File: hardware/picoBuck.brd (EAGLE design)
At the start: 22.8 x 27.3 mm, 23 parts, among them U1 AL8805, U2 AL8805, U3 AL8805

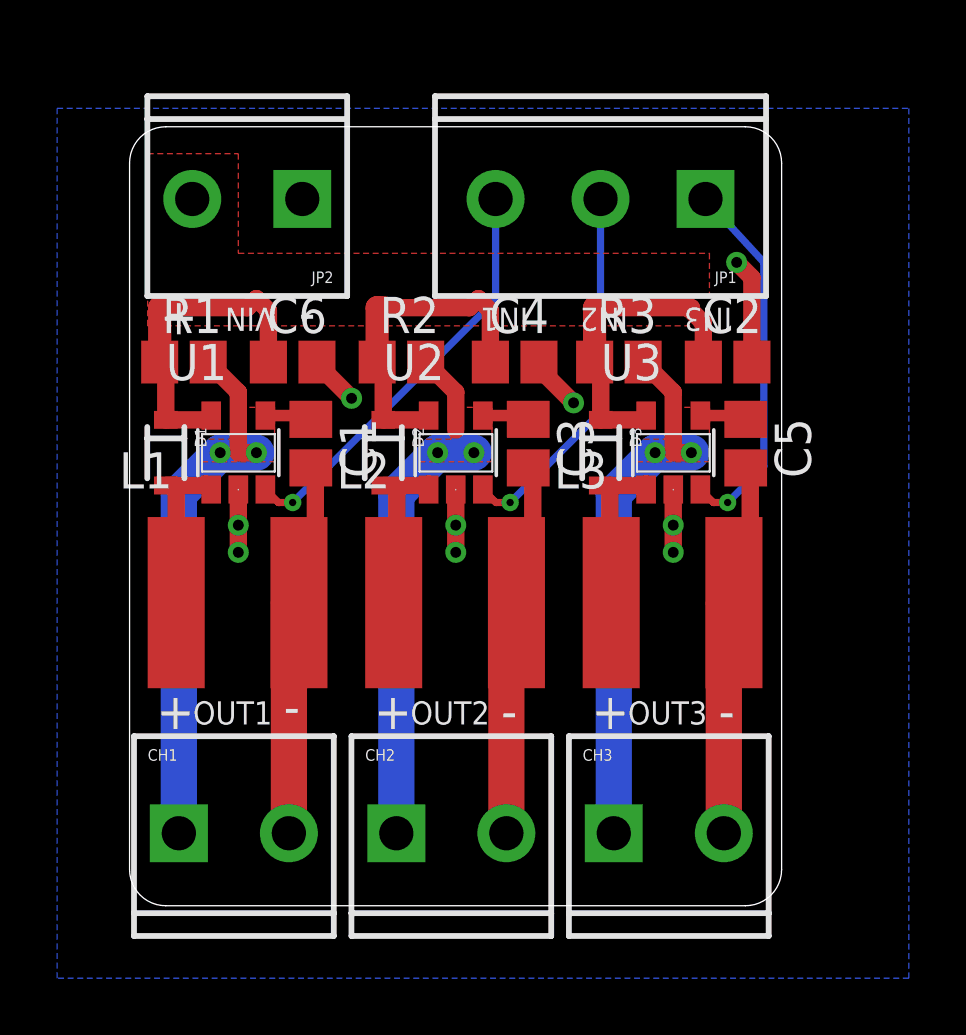
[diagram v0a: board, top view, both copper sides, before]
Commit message: Bringing board layout up to SparkFun DRC compliance
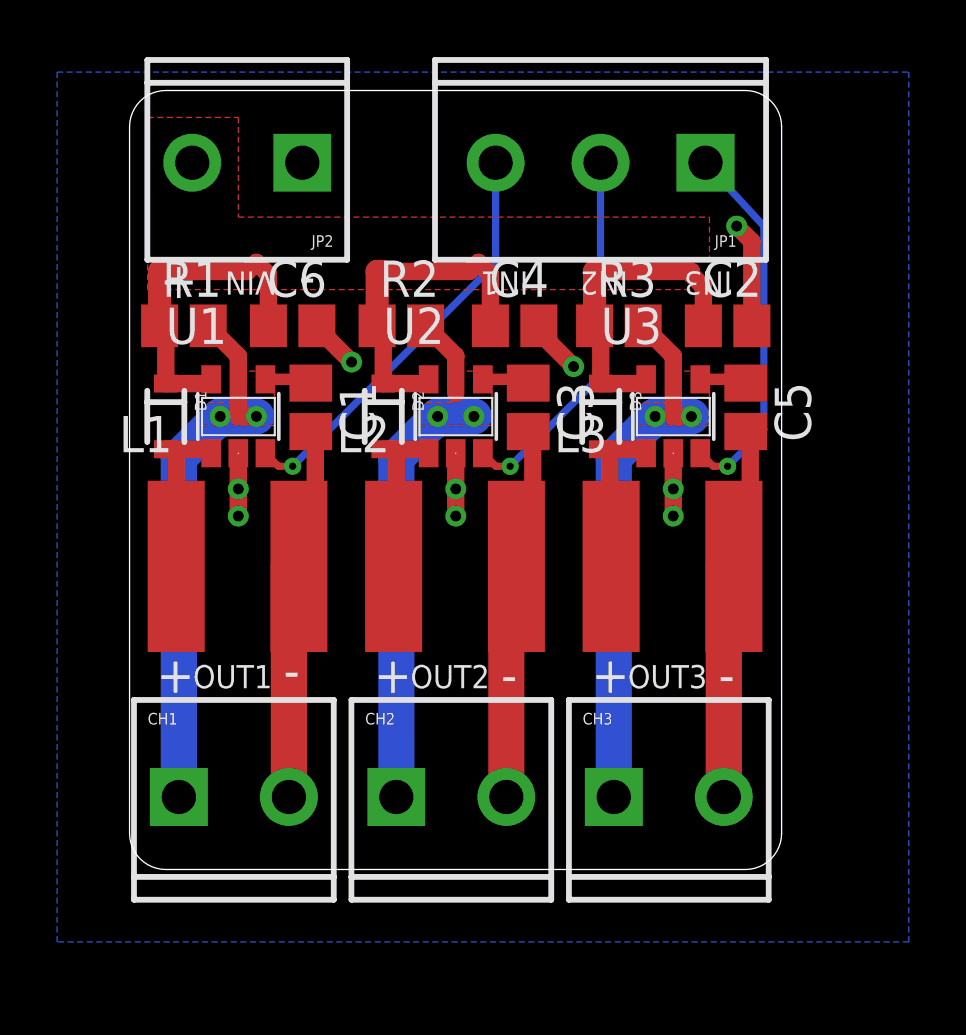
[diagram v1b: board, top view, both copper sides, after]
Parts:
- moved CH1 1.27 mm to (1.91, 2.54)
- moved CH2 1.27 mm to (9.53, 2.54)
- moved CH3 1.27 mm to (17.1, 2.54)
- moved C1 1.27 mm to (6.35, 16.2)
- moved C2 1.27 mm to (21.0, 19.1)
- moved C3 1.27 mm to (14.0, 16.2)
- moved C4 1.27 mm to (13.5, 19.1)
- moved C5 1.27 mm to (21.6, 16.2)
- moved C6 1.27 mm to (5.71, 19.1)
- moved D1 1.27 mm to (1.27, 15.9)
- moved D2 1.27 mm to (8.89, 15.9)
- moved D3 1.27 mm to (16.5, 15.9)
- moved JP1 1.27 mm to (20.0, 24.8)
- moved JP2 1.27 mm to (5.87, 24.8)
- moved L1 1.27 mm to (3.81, 10.8)
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
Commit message: Bringing up to standards- submitting this for review
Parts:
- added FRAME1: FRAME-LETTER, SparkFun-Aesthetics:CREATIVE_COMMONS
- added LOGO1: OSHW-LOGOS, SparkFun-Aesthetics:OSHW-LOGO-S
- added LOGO2: LOGO-SFENEW, SparkFun-Aesthetics:SFE-NEW-WEBLOGO
- moved L1 1.40 mm to (3.81, 9.40)
- moved L2 1.40 mm to (11.4, 9.40)
- moved L3 1.40 mm to (19.1, 9.40)
- moved CH1 1.27 mm to (1.91, 1.27)
- moved CH2 1.27 mm to (9.53, 1.27)
- moved CH3 1.27 mm to (17.1, 1.27)
- moved C1 1.27 mm to (6.35, 14.9)
- moved C2 1.27 mm to (21.0, 17.8)
- moved C3 1.27 mm to (14.0, 14.9)
- moved C4 1.27 mm to (13.5, 17.8)
- moved C5 1.27 mm to (21.6, 14.9)
- moved C6 1.27 mm to (5.71, 17.8)
- moved D1 1.27 mm to (1.27, 14.6)
- moved D2 1.27 mm to (8.89, 14.6)
- moved D3 1.27 mm to (16.5, 14.6)
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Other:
- board text removed: "Ethan Zonca"
- board text removed: "January 2013"
- board text removed: "Rev. 1"
